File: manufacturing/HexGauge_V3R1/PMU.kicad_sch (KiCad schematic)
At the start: 13 parts, among them Q1 Q_PMOS_GSD, U2 TPMP2359D

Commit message: Cleaned Up Schematic
Added Blockdiagram
Reannotated Symbols
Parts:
- renumbered C11 to C14, C13 to C15, C14 to C16, D1 to D2, R7 to R10, R8 to R11, R5 to R8, R6 to R9

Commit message: Updated Component Selection
Better availability
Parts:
- C14: LCSC Part # (none) -> C1532
- C15, C16: footprint Capacitor_SMD:C_1206_3216Metric -> Capacitor_SMD:C_1210_3225Metric; LCSC Part # C132148 -> C90142
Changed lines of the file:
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@@
       (effects (font (size 1.27 1.27)) (justify left))
     )
-    (property "Footprint" "Capacitor_SMD:C_1206_3216Metric" (at 174.9552 87.63 0)
+    (property "Footprint" "Capacitor_SMD:C_1210_3225Metric" (at 174.9552 87.63 0)
       (effects (font (size 1.27 1.27)) hide)
     )
@@
       (effects (font (size 1.27 1.27)) hide)
     )
-    (property "LCSC Part #" "C132148" (at 173.99 83.82 0)
+    (property "LCSC Part #" "C90142" (at 173.99 83.82 0)
       (effects (font (size 1.27 1.27)) hide)
     )
@@
       (effects (font (size 1.27 1.27)) (justify left))
     )
-    (property "Footprint" "Capacitor_SMD:C_1206_3216Metric" (at 79.7052 90.17 0)
+    (property "Footprint" "Capacitor_SMD:C_1210_3225Metric" (at 79.7052 90.17 0)
       (effects (font (size 1.27 1.27)) hide)
     )
@@
       (effects (font (size 1.27 1.27)) hide)
     )
-    (property "LCSC Part #" "C132148" (at 78.74 86.36 0)
+    (property "LCSC Part #" "C90142" (at 78.74 86.36 0)
       (effects (font (size 1.27 1.27)) hide)
     )
@@
       (effects (font (size 1.27 1.27)) hide)
     )
-    (property "LCSC Part #" "" (at 142.24 78.74 0)
-      (effects (font (size 1.27 1.27)) hide)
-    )
+    (property "LCSC Part #" "C1532" (at 142.24 78.74 0)
+      (effects (font (size 1.27 1.27)) hide)
+    )

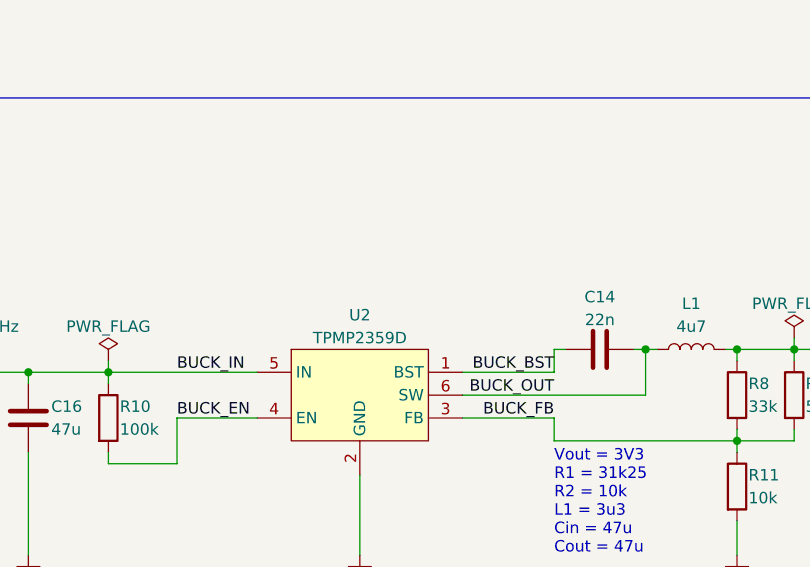
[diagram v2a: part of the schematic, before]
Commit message: Cost calculation
Find extended parts on mouser
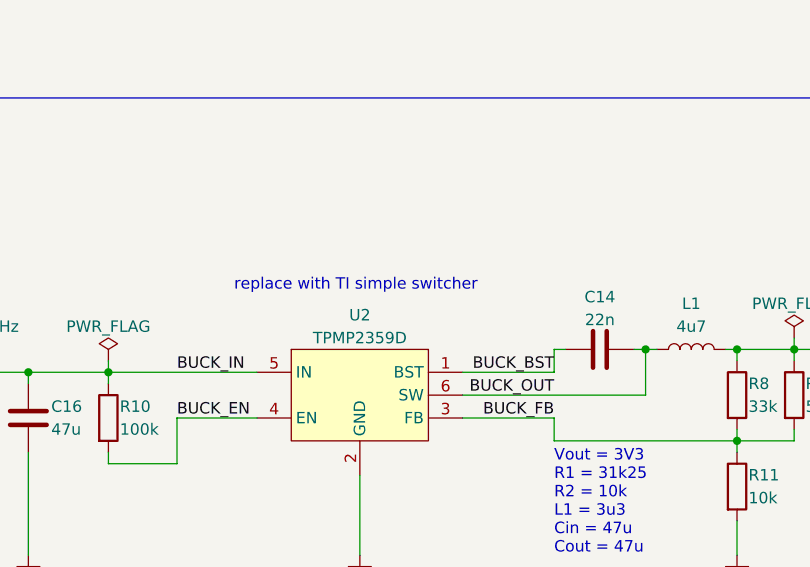
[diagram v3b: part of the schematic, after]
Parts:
- L1: footprint Inductor_SMD:L_7.3x7.3_H4.5 -> Inductor_SMD:L_Wuerth_WE-TPC-3816
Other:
- note added: "replace with TI simple switcher"
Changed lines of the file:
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@@
+    (effects (font (size 1.27 1.27)) (justify left bottom))
+  )
+  (text "replace with TI simple switcher" (at 101.6 72.39 0)
     (effects (font (size 1.27 1.27)) (justify left bottom))
   )
@@
       (effects (font (size 1.27 1.27)))
     )
-    (property "Footprint" "Inductor_SMD:L_7.3x7.3_H4.5" (at 152.4 78.74 0)
-      (effects (font (size 1.27 1.27)) hide)
-    )
+    (property "Footprint" "Inductor_SMD:L_Wuerth_WE-TPC-3816" (at 152.4 78.74 0)
+      (effects (font (size 1.27 1.27)) hide)
+    )
